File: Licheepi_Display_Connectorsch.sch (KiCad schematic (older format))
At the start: 1 part, among them P2 40pin_fpc_top_0_5mm

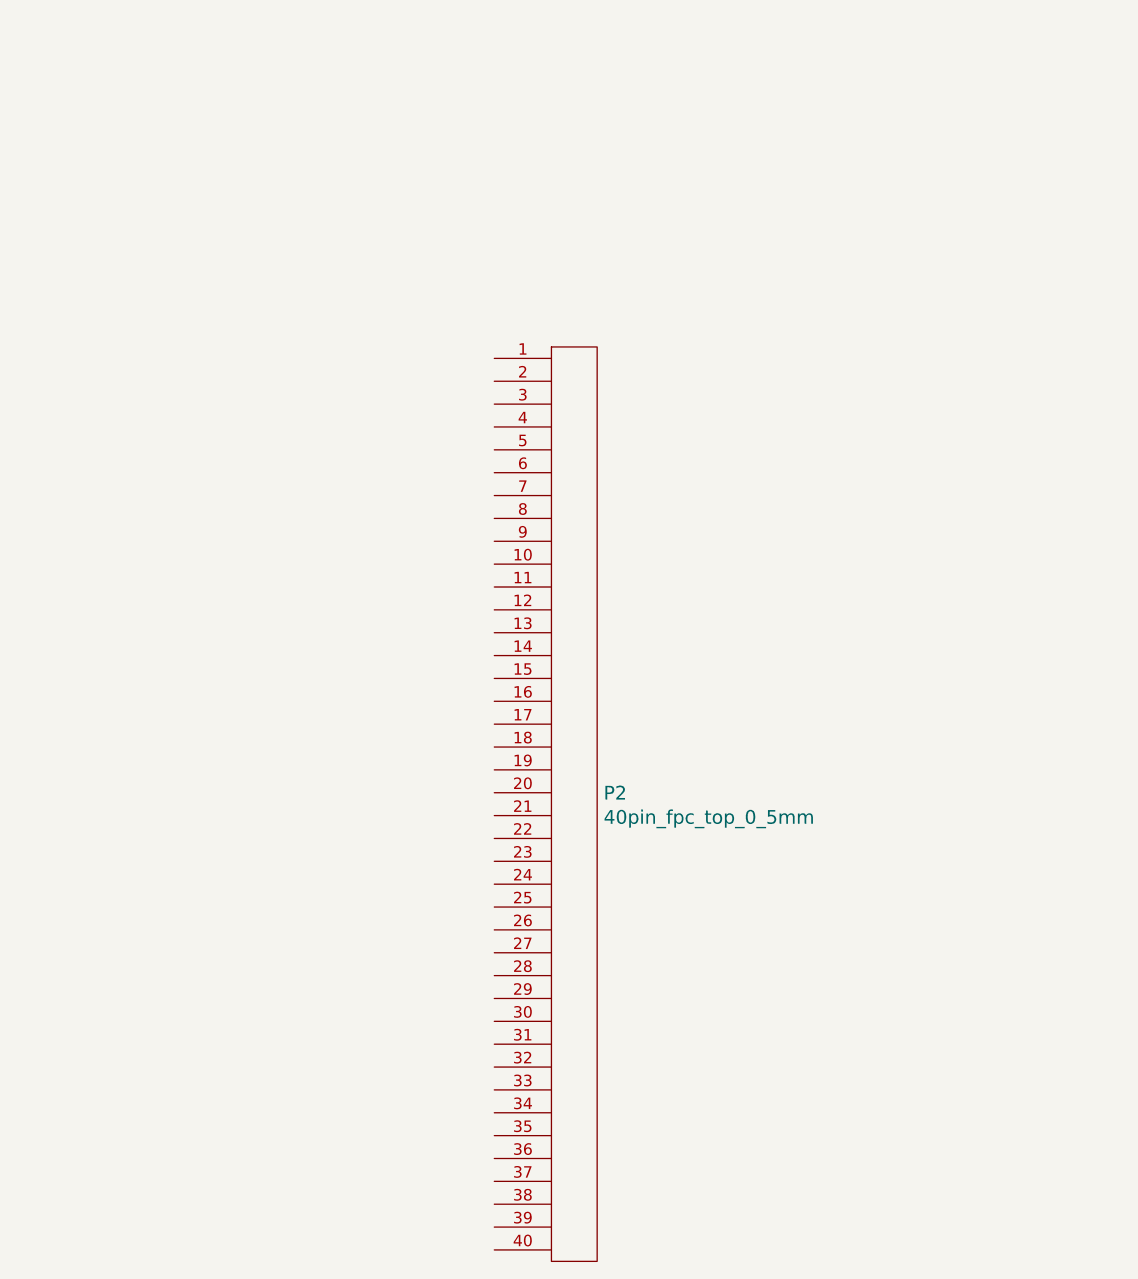
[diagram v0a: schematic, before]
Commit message: Filled hierarchical sheets
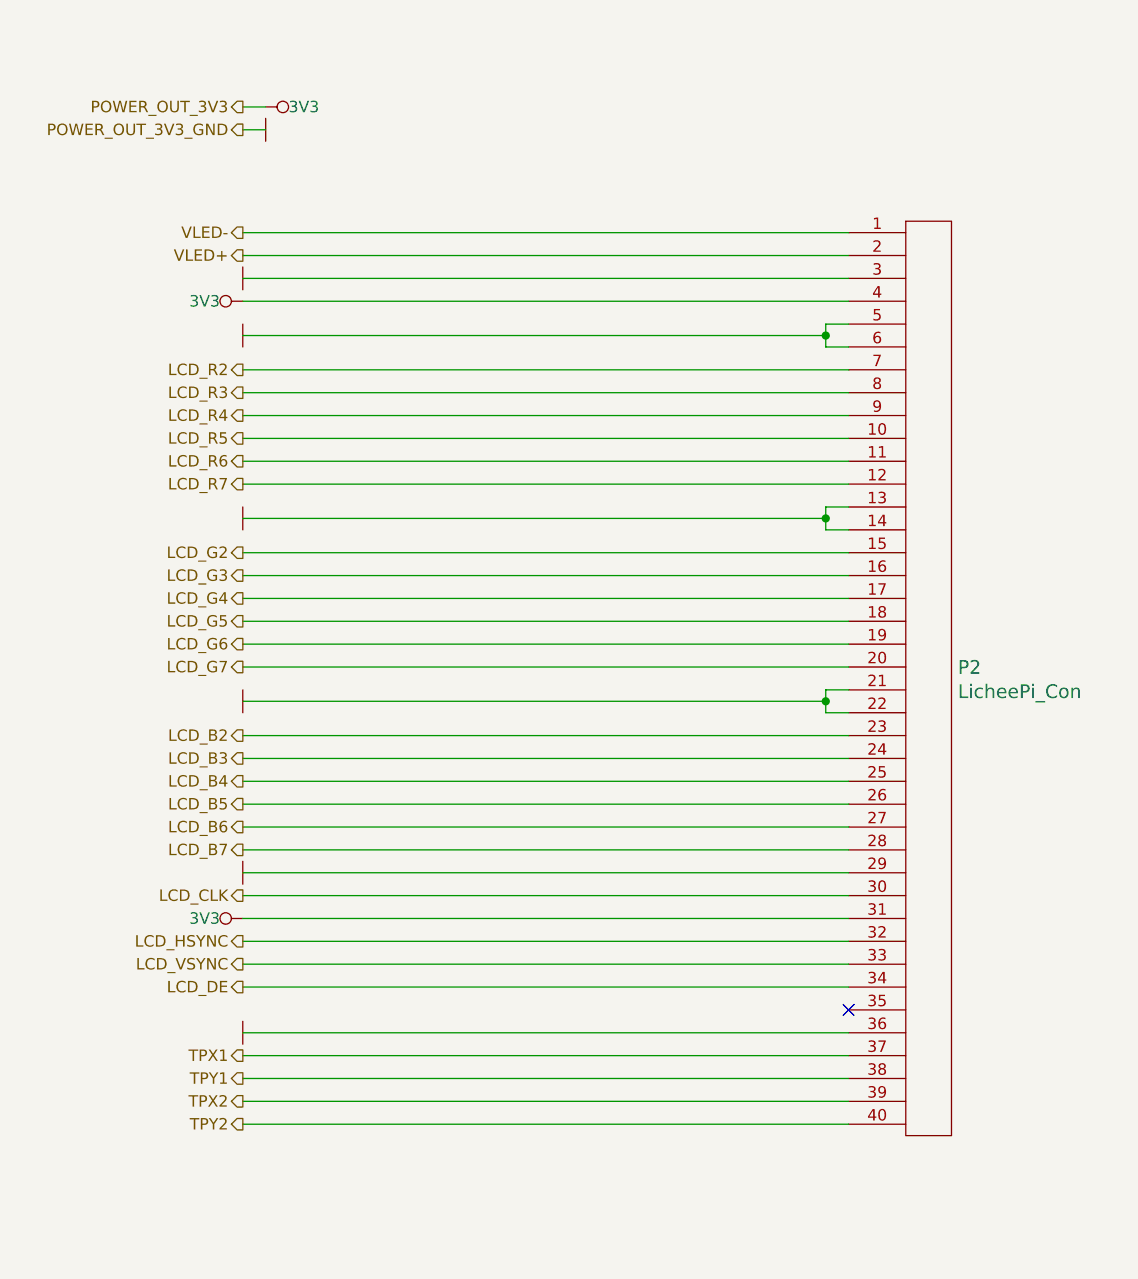
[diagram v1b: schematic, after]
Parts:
- P2: value 40pin_fpc_top_0_5mm -> LicheePi_Con
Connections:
- net VLED-: now reaches P2.1 (P1)
- net LCD_R5: now reaches P2.10 (P10)
- net LCD_R6: now reaches P2.11 (P1)
- net LCD_R7: now reaches P2.12 (P2)
- net GND: now reaches P2.13 (P3)
- net GND: now also P2.14 (P4), P2.21 (P1), P2.22 (P2), P2.29 (P9), P2.3 (P3), P2.36 (P6), P2.5 (P5), P2.6 (P6)
- net LCD_G2: now reaches P2.15 (P5)
- net LCD_G3: now reaches P2.16 (P6)
- net LCD_G4: now reaches P2.17 (P7)
- net LCD_G5: now reaches P2.18 (P8)
- net LCD_G6: now reaches P2.19 (P9)
- net VLED+: now reaches P2.2 (P2)
- net LCD_G7: now reaches P2.20 (P10)
- net LCD_B2: now reaches P2.23 (P3)
- net LCD_B3: now reaches P2.24 (P4)
- net LCD_B4: now reaches P2.25 (P5)
- net LCD_B5: now reaches P2.26 (P6)
- net LCD_B6: now reaches P2.27 (P7)
- net LCD_B7: now reaches P2.28 (P8)
- net LCD_CLK: now reaches P2.30 (P10)
- net 3V3: now reaches P2.31 (P1)
- net 3V3: now also P2.4 (P4)
- net LCD_HSYNC: now reaches P2.32 (P2)
- net LCD_VSYNC: now reaches P2.33 (P3)
- net LCD_DE: now reaches P2.34 (P4)
- net TPX1: now reaches P2.37 (P7)
- net TPY1: now reaches P2.38 (P8)
- net TPX2: now reaches P2.39 (P9)
- net TPY2: now reaches P2.40 (P10)
- net LCD_R2: now reaches P2.7 (P7)
- net LCD_R3: now reaches P2.8 (P8)
- net LCD_R4: now reaches P2.9 (P9)
- no-connect marks 0 -> 1
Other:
- moved on the sheet: P2

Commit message: Schematic ready, need check
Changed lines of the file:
@@
 $EndComp
 Wire Wire Line
-	6500 3050 6400 3050
+	6500 3050 6450 3050
 Wire Wire Line
 	6400 3150 6500 3150
+$Comp
+L power:PWR_FLAG #FLG0102
+U 1 1 5F13BA97
+P 6450 2950
+F 0 "#FLG0102" H 6450 3220 30  0001 C CNN
+F 1 "PWR_FLAG" H 6450 3208 30  0000 C CNN
+F 2 "" H 6450 2950 60  0000 C CNN
+F 3 "" H 6450 2950 60  0000 C CNN
+	1    6450 2950
+	1    0    0    -1
+$EndComp
+Wire Wire Line
+	6450 3050 6450 2950
+Connection ~ 6450 3050
+Wire Wire Line
+	6450 3050 6400 3050
 $EndSCHEMATC

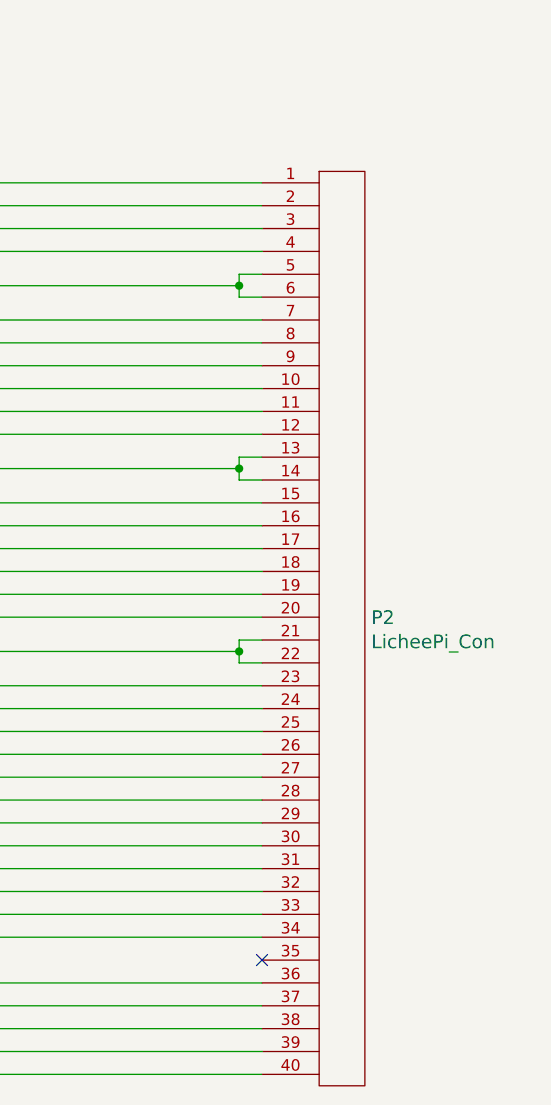
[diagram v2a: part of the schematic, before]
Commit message: Schematic finished, pcb tracking started
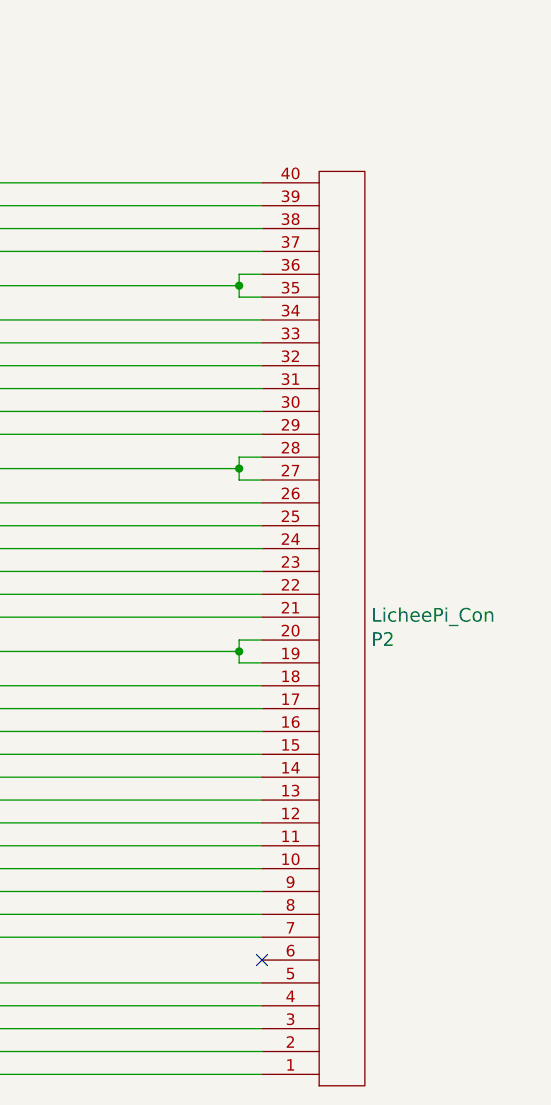
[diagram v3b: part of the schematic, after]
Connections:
- net 3V3: now also P2.10 (P10), P2.37 (P7); no longer P2.31 (P1), P2.4 (P4)
- net GND: now also P2.12 (P2), P2.19 (P9), P2.20 (P10), P2.27 (P7), P2.28 (P8), P2.35 (P5), P2.38 (P8); no longer P2.13 (P3), P2.14 (P4), P2.21 (P1), P2.22 (P2), P2.29 (P9), P2.3 (P3), P2.6 (P6)
- net LCD_B2: now also P2.18 (P8); no longer P2.23 (P3)
- net LCD_B3: now also P2.17 (P7); no longer P2.24 (P4)
- net LCD_B4: now also P2.16 (P6); no longer P2.25 (P5)
- net LCD_B5: now also P2.15 (P5); no longer P2.26 (P6)
- net LCD_B6: now also P2.14 (P4); no longer P2.27 (P7)
- net LCD_B7: now also P2.13 (P3); no longer P2.28 (P8)
- net LCD_CLK: now also P2.11 (P1); no longer P2.30 (P10)
- net LCD_DE: now also P2.7 (P7); no longer P2.34 (P4)
- net LCD_G2: now also P2.26 (P6); no longer P2.15 (P5)
- net LCD_G3: now also P2.25 (P5); no longer P2.16 (P6)
- net LCD_G4: now also P2.24 (P4); no longer P2.17 (P7)
- net LCD_G5: now also P2.23 (P3); no longer P2.18 (P8)
- net LCD_G6: now also P2.22 (P2); no longer P2.19 (P9)
- net LCD_G7: now also P2.21 (P1); no longer P2.20 (P10)
- net LCD_HSYNC: now also P2.9 (P9); no longer P2.32 (P2)
- net LCD_R2: now also P2.34 (P4); no longer P2.7 (P7)
- net LCD_R3: now also P2.33 (P3); no longer P2.8 (P8)
- net LCD_R4: now also P2.32 (P2); no longer P2.9 (P9)
- net LCD_R5: now also P2.31 (P1); no longer P2.10 (P10)
- net LCD_R6: now also P2.30 (P10); no longer P2.11 (P1)
- net LCD_R7: now also P2.29 (P9); no longer P2.12 (P2)
- net LCD_VSYNC: now also P2.8 (P8); no longer P2.33 (P3)
- net TPX1: now also P2.4 (P4); no longer P2.37 (P7)
- net TPX2: now also P2.2 (P2); no longer P2.39 (P9)
- net TPY1: now also P2.3 (P3); no longer P2.38 (P8)
- net TPY2: now also P2.1 (P1); no longer P2.40 (P10)
- net VLED+: now also P2.39 (P9); no longer P2.2 (P2)
- net VLED-: now also P2.40 (P10); no longer P2.1 (P1)
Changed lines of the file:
@@
 F 3 "Connectors/Fpc_Connectors/Components_Documentation/ZIFNZ0140CV-TR.pdf" H 9528 5439 60  0001 L CNN
 	1    9300 5550
-	1    0    0    -1
+	1    0    0    1
 $EndComp
 Wire Wire Line

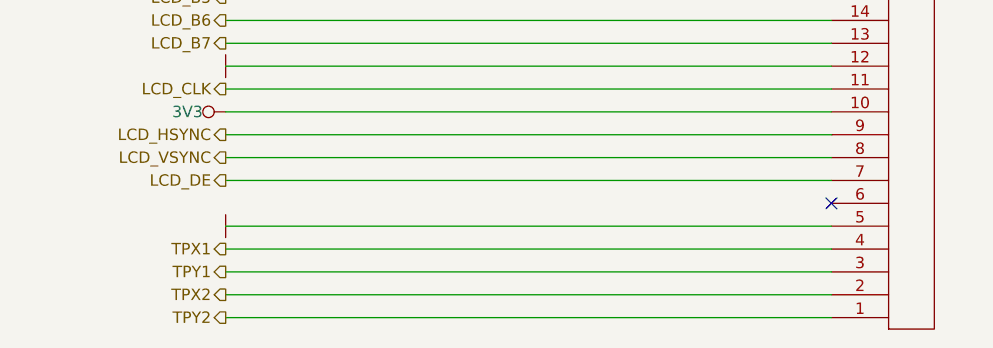
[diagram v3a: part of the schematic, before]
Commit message: Added new capacitive display
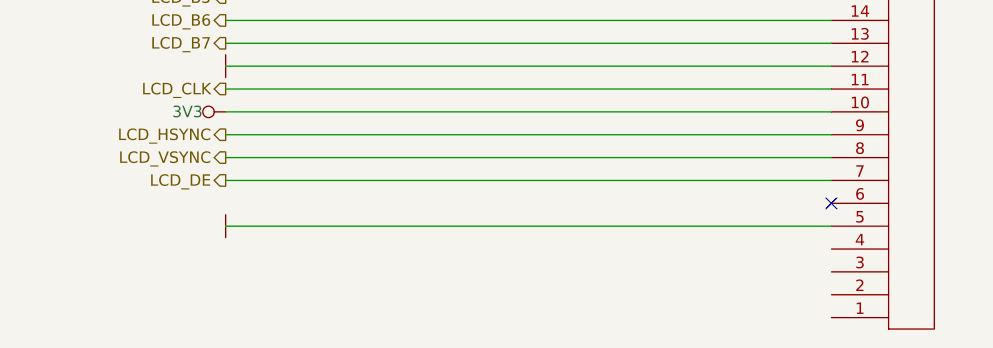
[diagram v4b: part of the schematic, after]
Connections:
- net TPX1: no longer names the net of P2.4 (P4)
- net TPX2: no longer names the net of P2.2 (P2)
- net TPY1: no longer names the net of P2.3 (P3)
- net TPY2: no longer names the net of P2.1 (P1)
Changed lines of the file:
@@
 LCD_DE
 NoConn ~ 9050 7000
-Wire Wire Line
-	9050 7100 6400 7100
-$Comp
-L power:GND #PWR0108
-U 1 1 5F0EF4AE
-P 6400 7100
-F 0 "#PWR0108" H 6400 7200 30  0001 C CNN
-F 1 "GND" H 6400 7000 30  0001 C CNN
-F 2 "" H 6400 7100 60  0000 C CNN
-F 3 "" H 6400 7100 60  0000 C CNN
-	1    6400 7100
-	0    1    1    0
-$EndComp
-Wire Wire Line
-	9050 7200 6400 7200
-Wire Wire Line
-	9050 7300 6400 7300
-Wire Wire Line
-	9050 7400 6400 7400
-Wire Wire Line
-	9050 7500 6400 7500
-Text HLabel 6400 7200 0    50   Output ~ 0
-TPX1
-Text HLabel 6400 7300 0    50   Output ~ 0
-TPY1
-Text HLabel 6400 7400 0    50   Output ~ 0
-TPX2
-Text HLabel 6400 7500 0    50   Output ~ 0
-TPY2
 Text HLabel 6400 3050 0    50   Output ~ 0
 POWER_OUT_3V3
@@
 Wire Wire Line
 	6450 3050 6400 3050
+$Comp
+L power:GND #PWR0108
+U 1 1 5F0EF4AE
+P 6400 7100
+F 0 "#PWR0108" H 6400 7200 30  0001 C CNN
+F 1 "GND" H 6400 7000 30  0001 C CNN
+F 2 "" H 6400 7100 60  0000 C CNN
+F 3 "" H 6400 7100 60  0000 C CNN
+	1    6400 7100
+	0    1    1    0
+$EndComp
+Wire Wire Line
+	9050 7100 6400 7100
 $EndSCHEMATC

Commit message: Generated gerbers
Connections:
- no-connect marks 1 -> 5
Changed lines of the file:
@@
 Wire Wire Line
 	9050 7100 6400 7100
+NoConn ~ 9050 7200
+NoConn ~ 9050 7300
+NoConn ~ 9050 7400
+NoConn ~ 9050 7500
 $EndSCHEMATC
